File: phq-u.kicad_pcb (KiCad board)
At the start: 4 copper layers, 130.4 x 75.4 mm, 110 parts, among them J1 18…56 V, J2 Voltage select, J3 MCU bypass, J4 3.3…24 V, J5 MCU disable, J6 TC2030, J7 I/O, J8 USB-C, Q1 NX138AK, U1 i7A4W033A033V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

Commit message: Connect TC2030 ground pad through via
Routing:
- net GND: track 95.4 -> 89.7 mm, vias 84 -> 85
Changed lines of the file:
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@@
   (via (at 171.5 111.9) (size 0.6) (drill 0.3) (layers "F.Cu" "B.Cu") (remove_unused_layers) (keep_end_layers) (free) (net 5))
   (via micro (at 143.599989 101.37) (size 0.6) (drill 0.3) (layers "F.Cu" "B.Cu") (remove_unused_layers) (keep_end_layers) (net 5))
+  (via micro (at 117.73 90.17) (size 0.6) (drill 0.3) (layers "F.Cu" "B.Cu") (remove_unused_layers) (net 5))
   (via micro (at 175.46 101.4) (size 0.6) (drill 0.3) (layers "F.Cu" "B.Cu") (remove_unused_layers) (keep_end_layers) (net 5))
   (via micro (at 147.31 100.38) (size 0.5) (drill 0.2) (layers "F.Cu" "B.Cu") (remove_unused_layers) (keep_end_layers) (net 5))
@@
   (segment (start 166.3 125.425) (end 167.374511 124.350489) (width 0.4) (layer "B.Cu") (net 5))
   (segment (start 187.81 75.945) (end 184.955 75.945) (width 0.4) (layer "B.Cu") (net 5))
+  (segment (start 117.735 90.17) (end 117.73 90.17) (width 0.4) (layer "B.Cu") (net 5))
   (segment (start 185.80657 76.795739) (end 185.805739 76.795739) (width 0.4) (layer "B.Cu") (net 5))
   (segment (start 144.3 125.425) (end 166.3 125.425) (width 0.4) (layer "B.Cu") (net 5))
   (segment (start 185.805739 76.795739) (end 184.955 75.945) (width 0.4) (layer "B.Cu") (net 5))
-  (segment (start 117.735 90.17) (end 118.291493 90.17) (width 0.4) (layer "B.Cu") (net 5))
-  (segment (start 118.291493 90.17) (end 121.65 93.528507) (width 0.4) (layer "B.Cu") (net 5))
   (segment (start 184.955 75.945) (end 151.349881 75.945) (width 0.4) (layer "B.Cu") (net 5))
   (segment (start 167.374511 124.350489) (end 167.374511 119.897961) (width 0.4) (layer "B.Cu") (net 5))
   (segment (start 104 116.2) (end 106.31 113.89) (width 0.4) (layer "B.Cu") (net 5))
-  (segment (start 121.65 93.528507) (end 121.65 93.95) (width 0.4) (layer "B.Cu") (net 5))
   (via micro (at 192.2 103.2) (size 0.6) (drill 0.3) (layers "F.Cu" "B.Cu") (remove_unused_layers) (keep_end_layers) (net 6))
   (via micro (at 192 112.9) (size 0.6) (drill 0.3) (layers "F.Cu" "B.Cu") (net 6))

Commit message: Add and adjust vias
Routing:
- net GND: track 89.7 -> 92.8 mm, vias 85 -> 95
- net /MCU/ESP_AD1_3: track 18.6 -> 20.6 mm
- net ESP_IO5: track 18.5 -> 19.9 mm
- net ESP_IO7: track 21.0 -> 22.2 mm
- net ESP_IO6: track 19.4 -> 20.6 mm
- net V_{out}: vias 24 -> 26
- net Net-(C7-Pad2): vias 23 -> 25
- net Earth: vias 114 -> 117
- net /Output caps/+: vias 14 -> 16

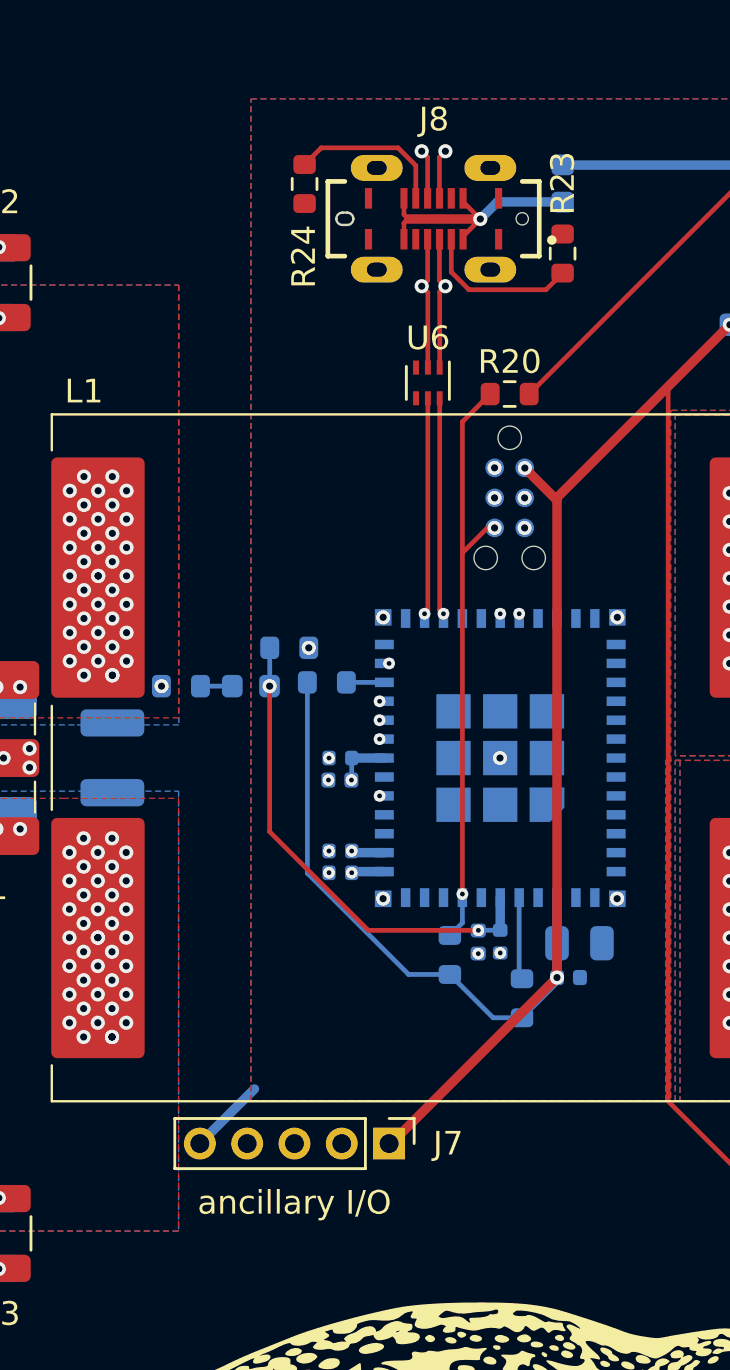
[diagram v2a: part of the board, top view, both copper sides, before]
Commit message: Replace generic I/O with LED connector
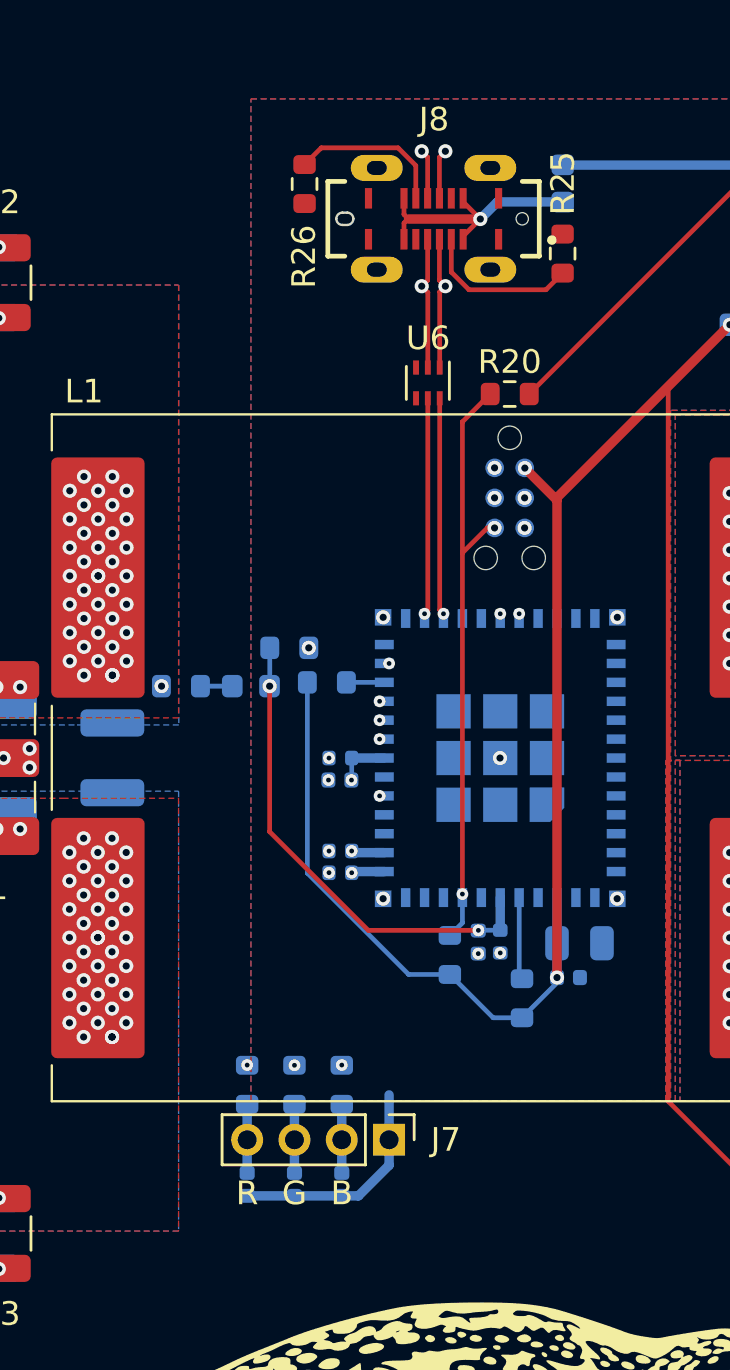
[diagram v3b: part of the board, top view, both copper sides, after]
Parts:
- added D10: 3V3, Diode_SMD:D_0402_1005Metric, B.Cu at (108.0, 117.9)
- added D11: 3V3, Diode_SMD:D_0402_1005Metric, B.Cu at (106.0, 117.9)
- added D9: 3V3, Diode_SMD:D_0402_1005Metric, B.Cu at (110.0, 117.9)
- added R23: 15 R, Resistor_SMD:R_0603_1608Metric, B.Cu at (110.0, 113.7)
- added R24: 15 R, Resistor_SMD:R_0603_1608Metric, B.Cu at (108.0, 113.7)
- added R27: 68 R, Resistor_SMD:R_0603_1608Metric, B.Cu at (106.0, 113.7)
- J7: value I/O -> LED; footprint Connector_PinHeader_2.00mm:PinHeader_1x05_P2.00mm_Vertical -> Connector_PinHeader_2.00mm:PinHeader_1x04_P2.00mm_Vertical
- moved G*** 0.50 mm to (135.0, 127.4)
- moved J7 0.16 mm to (112.0, 116.0)
- renumbered R23 to R25, R24 to R26
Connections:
- J7 pad 1: +3V3 -> GND
- J7 pad 2: ESP_IO5 -> Net-(D9-Pad1)
- J7 pad 3: ESP_IO6 -> Net-(D10-Pad1)
- J7 pad 4: ESP_IO7 -> Net-(D11-Pad1)
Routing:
- net +3V3: track 239.4 -> 229.5 mm
- net GND: track 92.8 -> 99.1 mm
- net ESP_IO5: track 19.9 -> 16.6 mm, vias 1 -> 2
- net ESP_IO6: track 20.6 -> 17.5 mm, vias 1 -> 2
- net ESP_IO7: track 22.2 -> 19.2 mm, vias 1 -> 2
- net Net-(D9-Pad1): track 0.00 -> 2.90 mm
- net Net-(D11-Pad1): track 0.00 -> 2.90 mm
- net Net-(D10-Pad1): track 0.00 -> 2.90 mm
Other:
- board text added: "B"
- board text added: "G"
- board text added: "R"
- board text removed: "ancillary I/O"

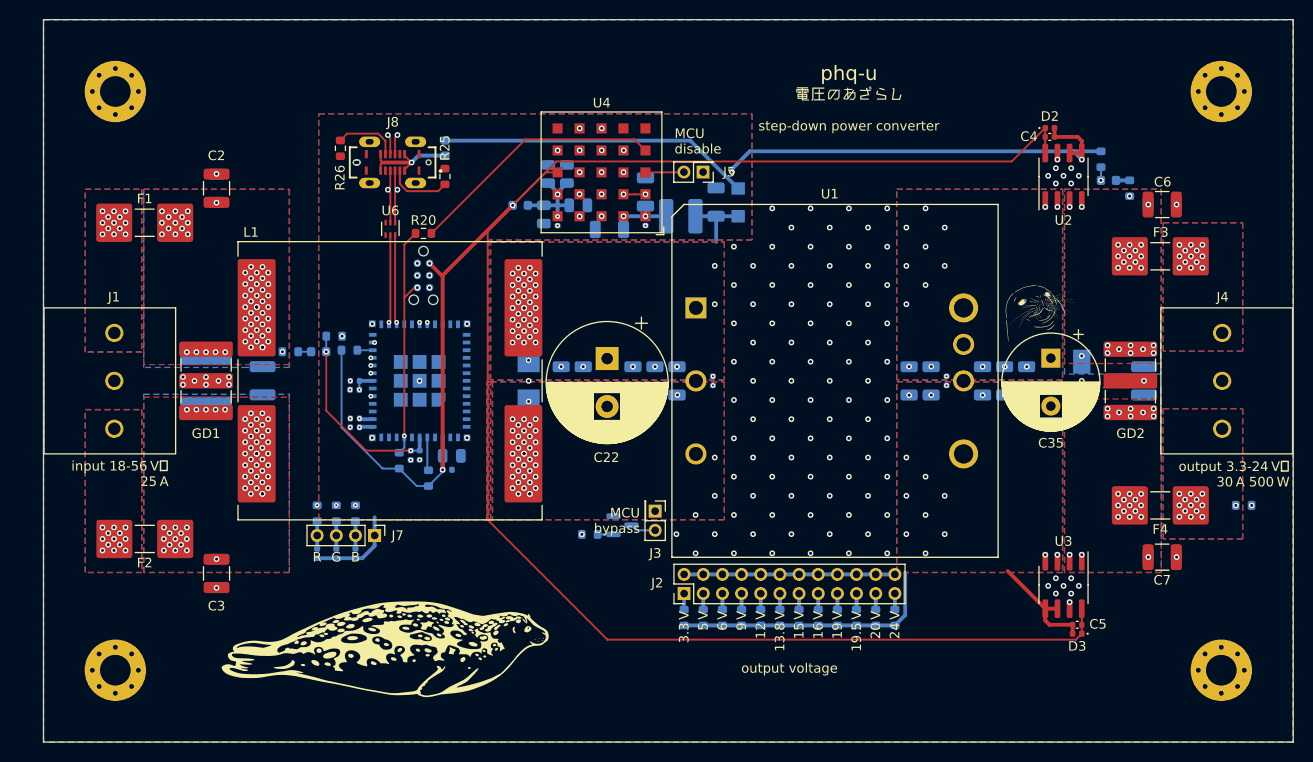
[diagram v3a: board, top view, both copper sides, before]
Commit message: Replace resistors with available variants
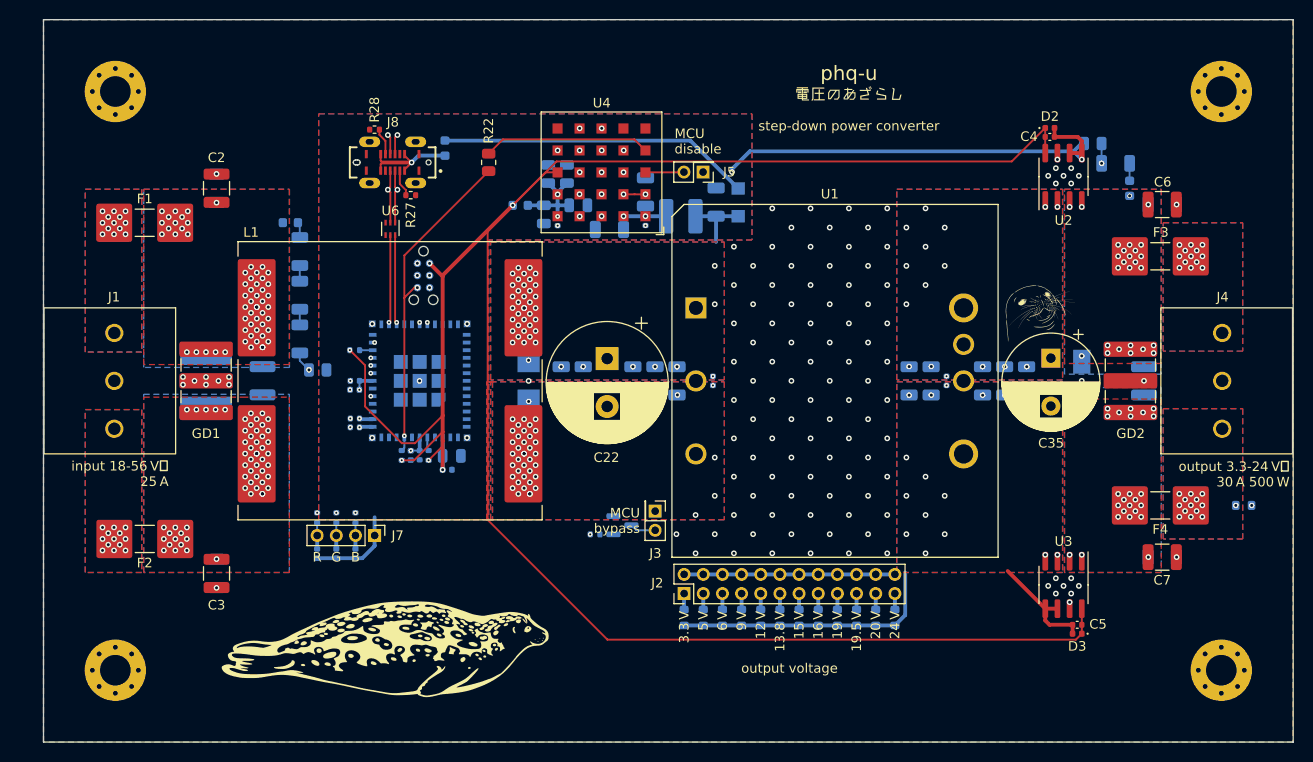
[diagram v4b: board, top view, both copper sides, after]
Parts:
- added R16: 5M, Resistor_SMD:R_1206_3216Metric, B.Cu at (104.2, 91.0)
- added R17: 2M4, Resistor_SMD:R_1206_3216Metric, B.Cu at (104.2, 95.5)
- Q1: value NX138AK -> NX138AKR
- R10: value 294 -> 287
- R15: value 25M -> 5M; footprint Resistor_SMD:R_0603_1608Metric -> Resistor_SMD:R_1206_3216Metric
- R18: renamed from R16; value 1M -> 499 k; footprint Resistor_SMD:R_0603_1608Metric -> Resistor_SMD:R_0805_2012Metric
- R19: renamed from R17; footprint Resistor_SMD:R_0603_1608Metric -> Resistor_SMD:R_1206_3216Metric
- R2: value 8k76 -> 8k66
- R20: renamed from R18; value 500k -> 499k; footprint Resistor_SMD:R_0603_1608Metric -> Resistor_SMD:R_0805_2012Metric
- R21: renamed from R19; footprint Resistor_SMD:R_0603_1608Metric -> Resistor_SMD:R_0402_1005Metric
- R22: renamed from R20; value 0 -> 10 m; footprint Resistor_SMD:R_0603_1608Metric -> Resistor_SMD:R_0805_2012Metric
- R23: renamed from R21; footprint Resistor_SMD:R_0603_1608Metric -> Resistor_SMD:R_0402_1005Metric
- R24: renamed from R22; footprint Resistor_SMD:R_0603_1608Metric -> Resistor_SMD:R_0402_1005Metric
- R25: renamed from R23; footprint Resistor_SMD:R_0603_1608Metric -> Resistor_SMD:R_0402_1005Metric
- R26: renamed from R24; footprint Resistor_SMD:R_0603_1608Metric -> Resistor_SMD:R_0402_1005Metric
- R27: renamed from R25; footprint Resistor_SMD:R_0603_1608Metric -> Resistor_SMD:R_0402_1005Metric
- R28: renamed from R26; footprint Resistor_SMD:R_0603_1608Metric -> Resistor_SMD:R_0402_1005Metric
- R29: renamed from R27; footprint Resistor_SMD:R_0603_1608Metric -> Resistor_SMD:R_0402_1005Metric
- R7: footprint Resistor_SMD:R_0603_1608Metric -> Resistor_SMD:R_0402_1005Metric
- moved F5 13.8 mm to (103.2, 83.4)
- moved R15 10.5 mm to (104.2, 86.4), turned to -90 degrees
- moved R22 10.1 mm to (123.9, 77.1), turned to -90 degrees
- moved R27 4.07 mm to (115.8, 80.5), turned to 0 degrees
- moved R28 4.06 mm to (112.0, 73.7), turned to 180 degrees
- moved R18 3.92 mm to (106.1, 98.8)
- moved R19 2.98 mm to (189.3, 77.2), turned to 180 degrees
- moved R21 2.38 mm to (117.6, 107.7)
- moved F6 2.36 mm to (190.8, 79.8), turned to 90 degrees
- moved R20 1.85 mm to (187.0, 75.1), turned to 180 degrees
- moved R23 0.60 mm to (114.8, 107.7)
- moved R7 0.55 mm to (135.0, 115.9)
- moved R24 0.55 mm to (109.9, 96.7)
- moved R25 0.47 mm to (110.0, 114.2)
- moved R26 0.47 mm to (108.0, 114.2)
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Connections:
- F5 pad 1: Net-(F5-Pad1) -> V_{in}
- F5 pad 2: /MCU/ESP_AD1_3 -> Net-(F5-Pad2)
- F6 pad 1: Net-(F6-Pad1) -> V_{out}
- F6 pad 2: /MCU/ESP_AD1_4 -> Net-(F6-Pad2)
- R15 pad 1: V_{in} -> Net-(F5-Pad2)
- R15 pad 2: Net-(F5-Pad1) -> Net-(R15-Pad2)
- R19 pad 1: V_{out} -> Net-(F6-Pad2)
- R19 pad 2: Net-(F6-Pad1) -> /MCU/ESP_AD1_4
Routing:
- net /MCU/ESP_EN: track 25.2 -> 34.7 mm
- net Net-(R22-Pad1): track 26.9 -> 17.5 mm
- net Net-(J8-PadA5): track 6.70 -> 2.82 mm
- net Net-(J8-PadB5): track 6.69 -> 2.82 mm
- net +3V3: track 229.5 -> 233.3 mm, vias 3 -> 6
- net /MCU/ESP_AD1_4: track 90.1 -> 92.6 mm
- net /MCU/ESP_AD1_3: track 20.6 -> 18.6 mm
- net Net-(R21-Pad2): track 3.31 -> 1.42 mm
- net Net-(F6-Pad2): track 0.00 -> 1.81 mm
- net Net-(Q1-Pad1): track 1.65 -> 0.00 mm
- net Net-(R15-Pad2): track 0.00 -> 1.64 mm
- net Net-(R16-Pad2): track 0.00 -> 1.64 mm
- net Net-(F5-Pad2): track 0.00 -> 1.63 mm
- net GND: track 99.1 -> 97.7 mm, vias 95 -> 92
- net Net-(F6-Pad1): track 1.42 -> 0.00 mm
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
